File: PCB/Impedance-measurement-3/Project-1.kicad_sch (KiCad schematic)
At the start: 74 parts, among them J2 USB_C_Receptacle, U1 STM32F303CCT6, U2 W25Q32JVSSIQ, U5 LM7805_TO220, U9 OPA4141AID

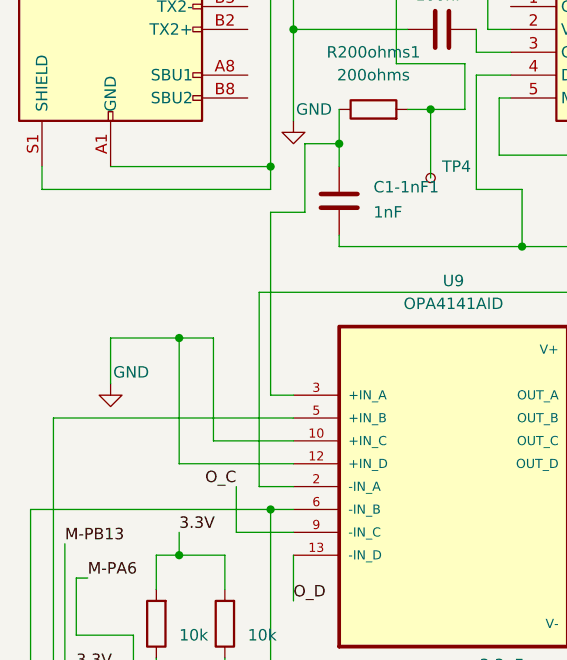
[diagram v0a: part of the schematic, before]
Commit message: schematic and layout changed second time in 26/7/2026
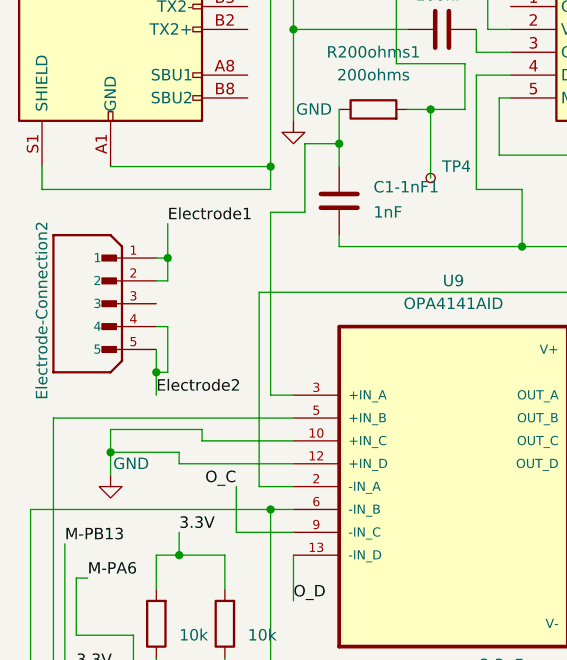
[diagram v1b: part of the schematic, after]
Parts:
- added Electrode-Connection2: Cable-connector B5B-XH-A_LF__SN_, Connector:JST_B5B-XH-A_LF__SN_, symbol 5 pos cable connector B5B-XH-A_LF__SN_:B5B-XH-A_LF__SN_
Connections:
- net Electrode1: now also Electrode-Connection2.1, Electrode-Connection2.2
- net Electrode2: now also Electrode-Connection2.4, Electrode-Connection2.5
